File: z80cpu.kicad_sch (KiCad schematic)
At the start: 2 parts

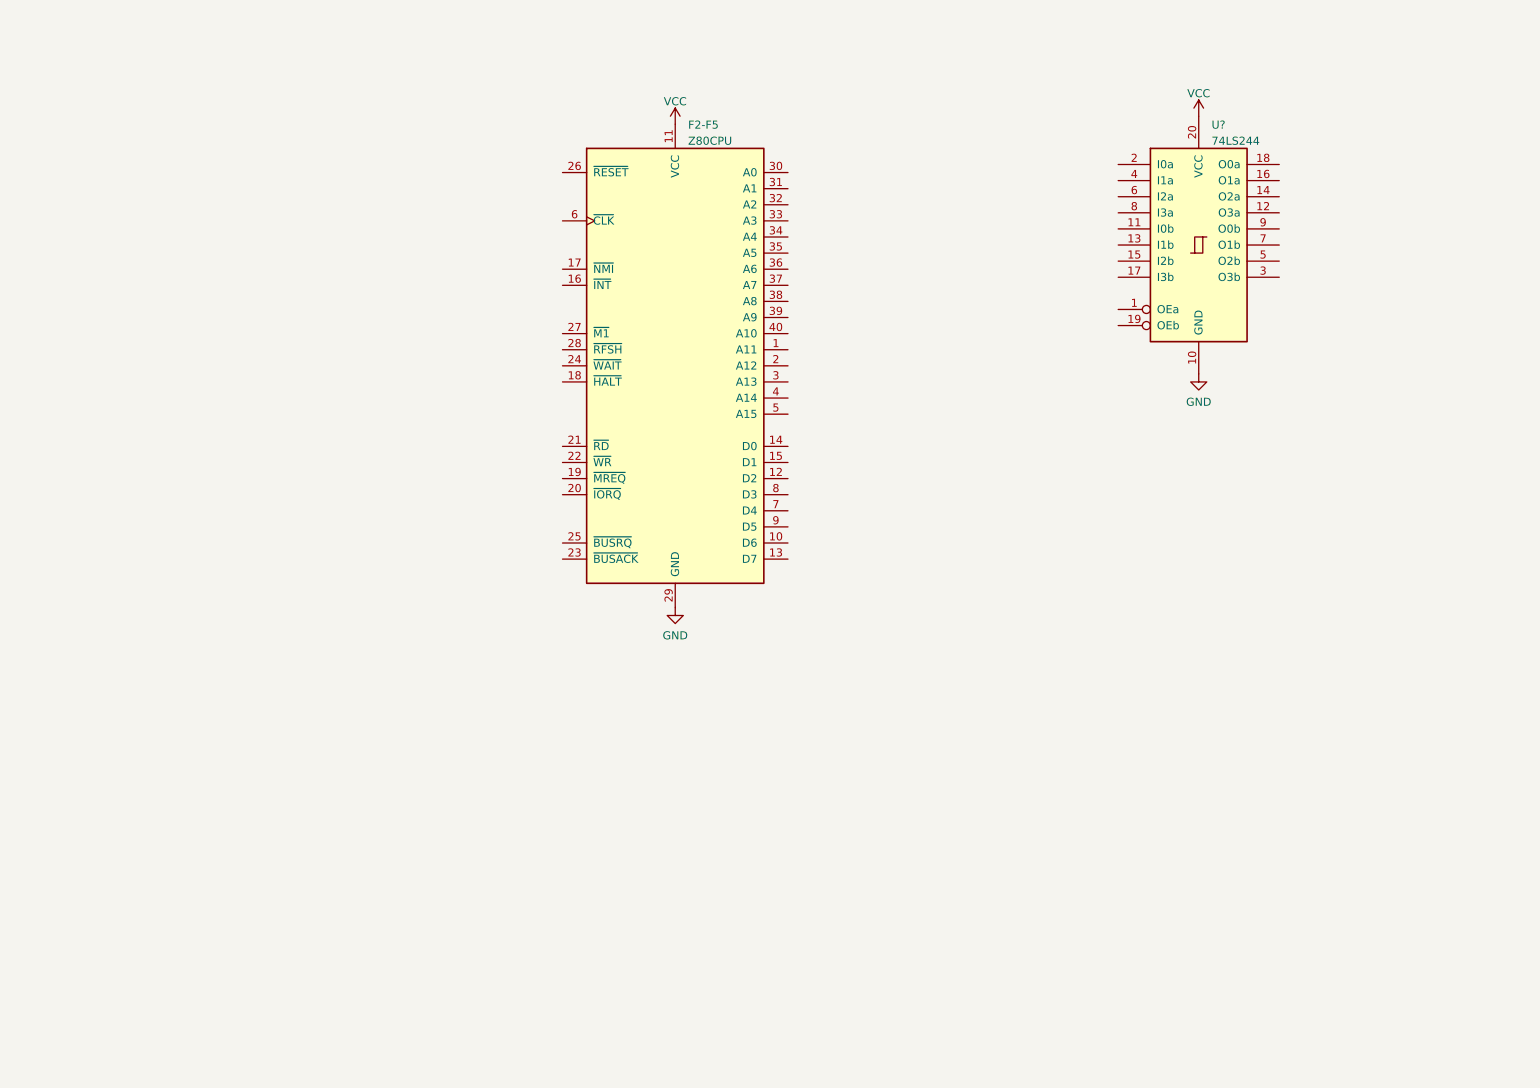
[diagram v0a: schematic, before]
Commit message: Added bus buffers (or their placeholders) to z80cpu schematic
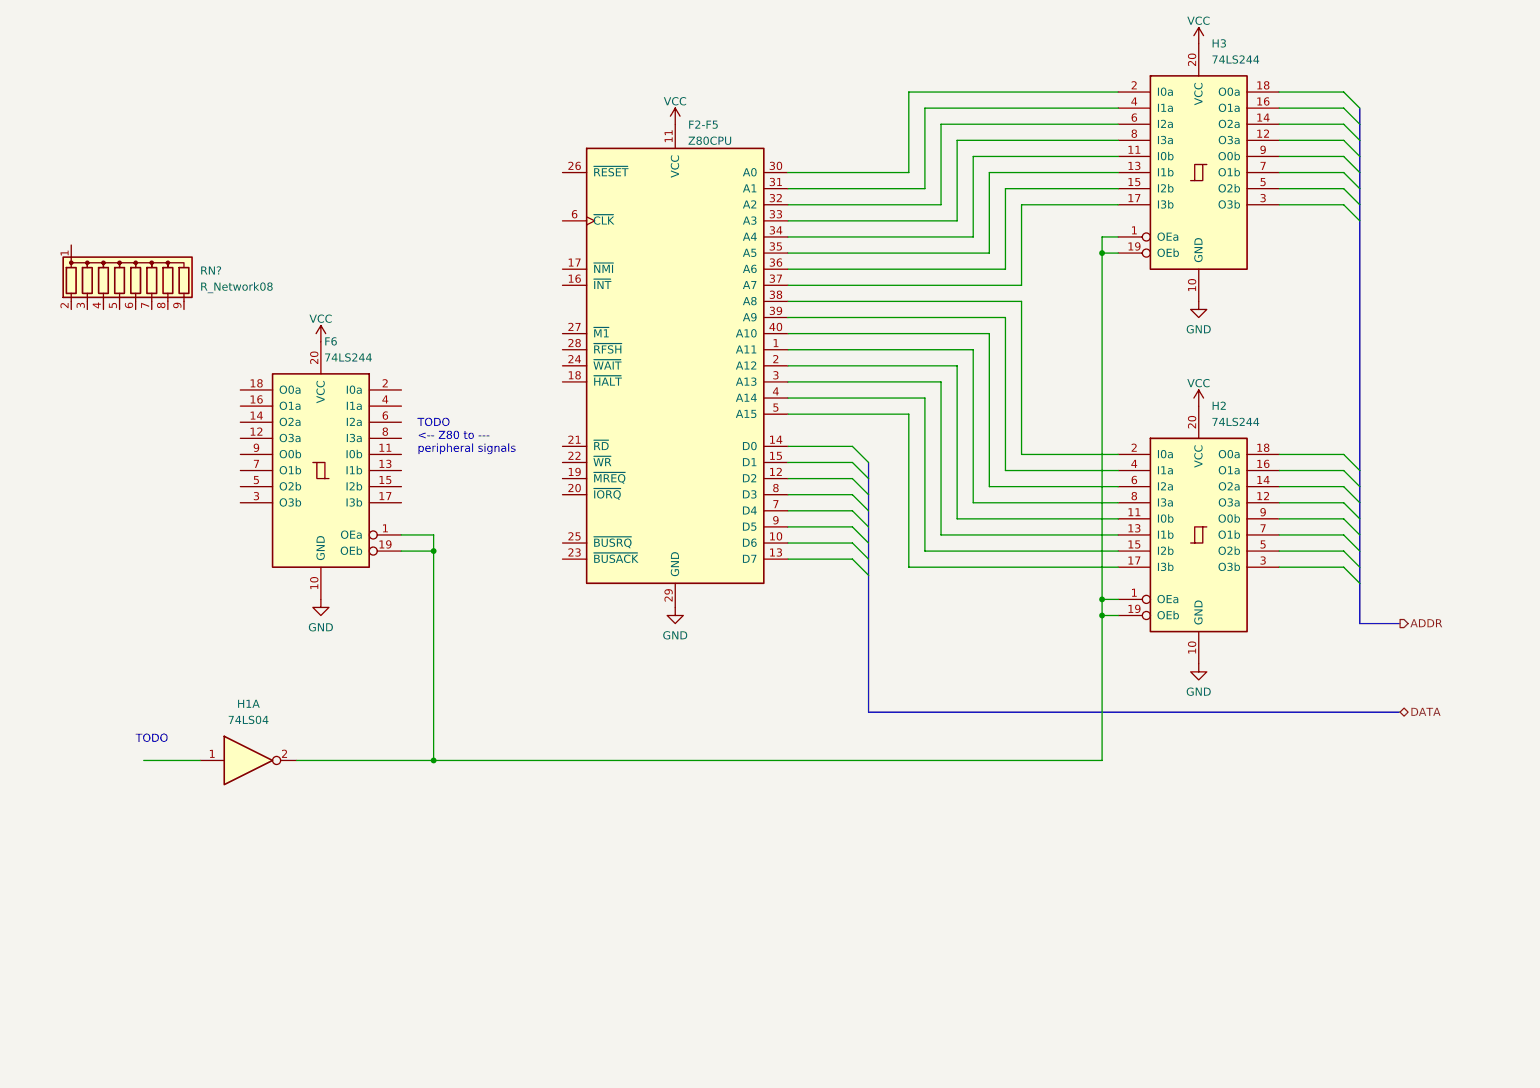
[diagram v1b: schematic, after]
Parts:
- added F6, H2: 74LS244, symbol 74xx:74LS244
- added H1: 74LS04, symbol 74xx:74LS04
- added RN?: R_Network08, Resistor_THT:R_Array_SIP9, symbol Device:R_Network08
- gave numbers to parts that had none: 1
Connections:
- net GND: now also F6.10 (GND), H2.10 (GND)
- net VCC: now also F6.20 (VCC), H2.20 (VCC)
- net at H3.1 (OEa): now also H3.19 (OEb), F6.1 (OEa), F6.19 (OEb), H1.2, H2.1 (OEa), H2.19 (OEb)
- net at H3.11 (I0b): now also F2-F5.34 (A4)
- net at H3.13 (I1b): now also F2-F5.35 (A5)
- net at H3.15 (I2b): now also F2-F5.36 (A6)
- net at H3.17 (I3b): now also F2-F5.37 (A7)
- net at H3.2 (I0a): now also F2-F5.30 (A0)
- net at H3.4 (I1a): now also F2-F5.31 (A1)
- net at H3.6 (I2a): now also F2-F5.32 (A2)
- net at H3.8 (I3a): now also F2-F5.33 (A3)
- net at F2-F5.1 (A11): now also H2.8 (I3a)
- net at F2-F5.2 (A12): now also H2.11 (I0b)
- net at F2-F5.3 (A13): now also H2.13 (I1b)
- net at F2-F5.38 (A8): now also H2.2 (I0a)
- net at F2-F5.39 (A9): now also H2.4 (I1a)
- net at F2-F5.4 (A14): now also H2.15 (I2b)
- net at F2-F5.40 (A10): now also H2.6 (I2a)
- net at F2-F5.5 (A15): now also H2.17 (I3b)
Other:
- note added: "TODO"
- note added: "TODO <-- Z80 to --- peripheral signals"
- moved on the sheet: H3

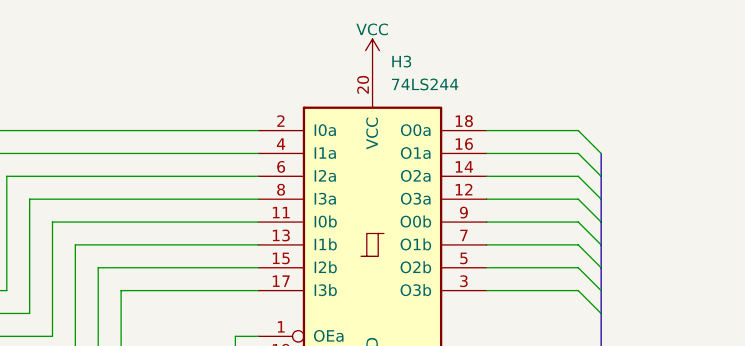
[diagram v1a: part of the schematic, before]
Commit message: Upgraded to kicad 7
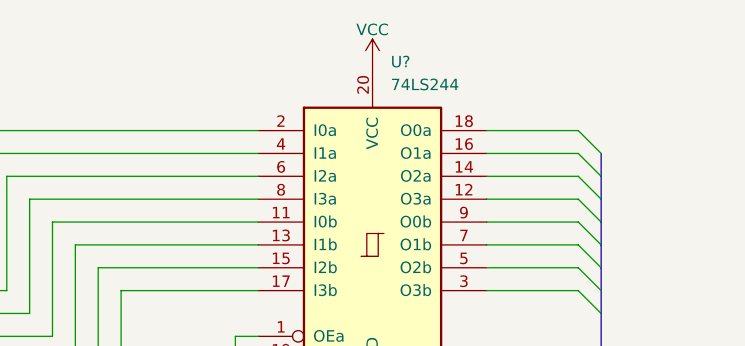
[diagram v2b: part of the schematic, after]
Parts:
- renumbered H3 to U?

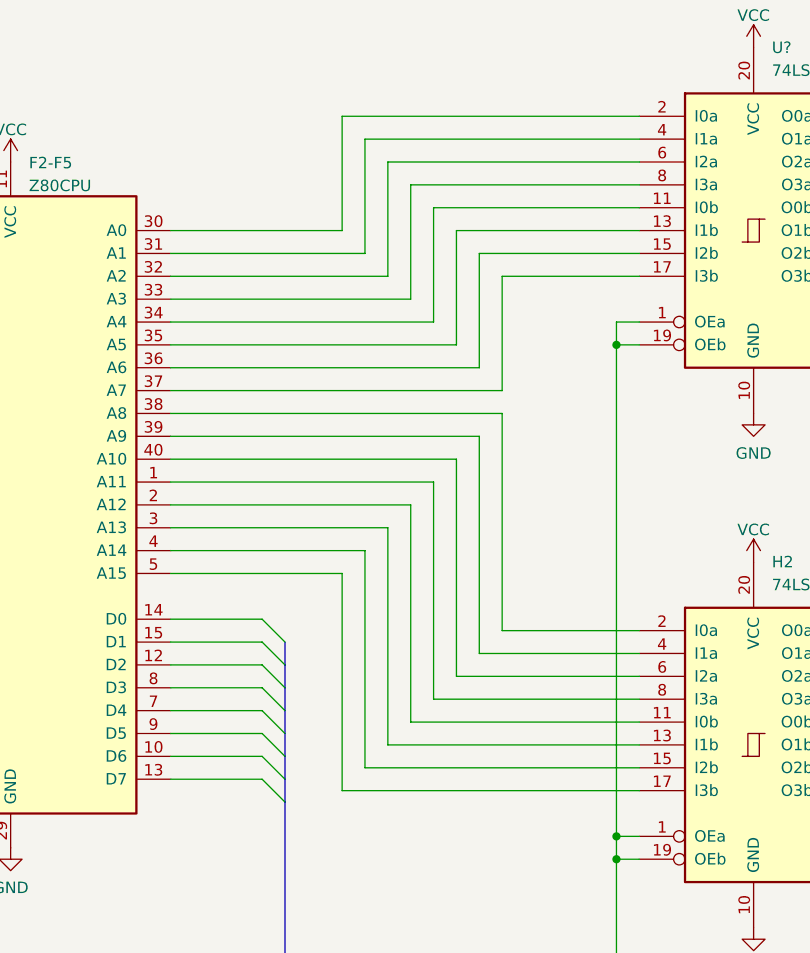
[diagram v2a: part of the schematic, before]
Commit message: Fixed address connection from Z80 to buffers
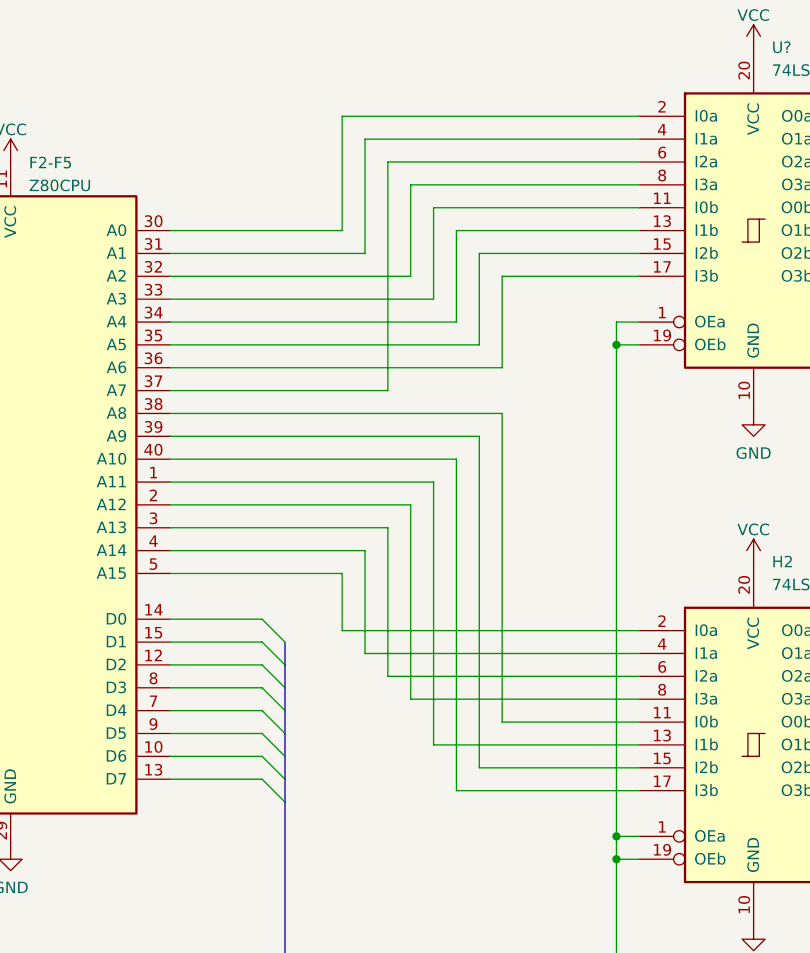
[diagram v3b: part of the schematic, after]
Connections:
- net at U?.11 (I0b): now also F2-F5.33 (A3); no longer F2-F5.34 (A4)
- net at U?.13 (I1b): now also F2-F5.34 (A4); no longer F2-F5.35 (A5)
- net at U?.15 (I2b): now also F2-F5.35 (A5); no longer F2-F5.36 (A6)
- net at U?.17 (I3b): now also F2-F5.36 (A6); no longer F2-F5.37 (A7)
- net at U?.6 (I2a): now also F2-F5.37 (A7); no longer F2-F5.32 (A2)
- net at U?.8 (I3a): now also F2-F5.32 (A2); no longer F2-F5.33 (A3)
- net at F2-F5.1 (A11): now also H2.13 (I1b); no longer H2.8 (I3a)
- net at F2-F5.2 (A12): now also H2.8 (I3a); no longer H2.11 (I0b)
- net at F2-F5.3 (A13): now also H2.6 (I2a); no longer H2.13 (I1b)
- net at F2-F5.38 (A8): now also H2.11 (I0b); no longer H2.2 (I0a)
- net at F2-F5.39 (A9): now also H2.15 (I2b); no longer H2.4 (I1a)
- net at F2-F5.4 (A14): now also H2.4 (I1a); no longer H2.15 (I2b)
- net at F2-F5.40 (A10): now also H2.17 (I3b); no longer H2.6 (I2a)
- net at F2-F5.5 (A15): now also H2.2 (I0a); no longer H2.17 (I3b)
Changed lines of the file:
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@@
     (stroke (width 0) (type default))
   )
-  (wire (pts (xy 185.42 99.06) (xy 157.48 99.06))
+  (wire (pts (xy 185.42 99.06) (xy 162.56 99.06))
     (stroke (width 0) (type default))
   )
@@
     (stroke (width 0) (type default))
   )
-  (wire (pts (xy 154.94 101.6) (xy 185.42 101.6))
+  (wire (pts (xy 157.48 91.44) (xy 157.48 74.93))
     (stroke (width 0) (type default))
   )
@@
     (stroke (width 0) (type default))
   )
-  (wire (pts (xy 170.18 46.99) (xy 170.18 59.69))
+  (wire (pts (xy 170.18 46.99) (xy 170.18 57.15))
     (stroke (width 0) (type default))
   )
@@
     (stroke (width 0) (type default))
   )
+  (wire (pts (xy 160.02 46.99) (xy 160.02 36.83))
+    (stroke (width 0) (type default))
+  )
   (bus (pts (xy 146.05 105.41) (xy 146.05 127))
     (stroke (width 0) (type default))
   )
+  (wire (pts (xy 162.56 49.53) (xy 162.56 39.37))
+    (stroke (width 0) (type default))
+  )
+  (wire (pts (xy 170.18 96.52) (xy 185.42 96.52))
+    (stroke (width 0) (type default))
+  )
+  (wire (pts (xy 170.18 62.23) (xy 170.18 96.52))
+    (stroke (width 0) (type default))
+  )
+  (wire (pts (xy 133.35 49.53) (xy 162.56 49.53))
+    (stroke (width 0) (type default))
+  )
   (wire (pts (xy 167.64 64.77) (xy 133.35 64.77))
     (stroke (width 0) (type default))
@@
     (stroke (width 0) (type default))
   )
-  (wire (pts (xy 133.35 49.53) (xy 160.02 49.53))
-    (stroke (width 0) (type default))
-  )
   (wire (pts (xy 152.4 29.21) (xy 185.42 29.21))
     (stroke (width 0) (type default))
@@
     (stroke (width 0) (type default))
   )
-  (wire (pts (xy 167.64 88.9) (xy 167.64 64.77))
-    (stroke (width 0) (type default))
-  )
   (wire (pts (xy 185.42 52.07) (xy 182.88 52.07))
     (stroke (width 0) (type default))
   )
-  (wire (pts (xy 160.02 72.39) (xy 160.02 96.52))
+  (wire (pts (xy 160.02 72.39) (xy 160.02 93.98))
     (stroke (width 0) (type default))
   )
@@
     (stroke (width 0) (type default))
   )
-  (wire (pts (xy 162.56 93.98) (xy 162.56 69.85))
-    (stroke (width 0) (type default))
-  )
-  (wire (pts (xy 170.18 59.69) (xy 133.35 59.69))
-    (stroke (width 0) (type default))
-  )
   (bus (pts (xy 223.52 39.37) (xy 223.52 41.91))
     (stroke (width 0) (type default))
@@
     (stroke (width 0) (type default))
   )
-  (wire (pts (xy 185.42 104.14) (xy 152.4 104.14))
+  (wire (pts (xy 167.64 64.77) (xy 167.64 101.6))
+    (stroke (width 0) (type default))
+  )
+  (wire (pts (xy 185.42 104.14) (xy 165.1 104.14))
     (stroke (width 0) (type default))
   )
@@
     (stroke (width 0) (type default))
   )
+  (wire (pts (xy 152.4 86.36) (xy 152.4 80.01))
+    (stroke (width 0) (type default))
+  )
   (wire (pts (xy 182.88 52.07) (xy 182.88 54.61))
     (stroke (width 0) (type default))
@@
     (stroke (width 0) (type default))
   )
-  (wire (pts (xy 185.42 93.98) (xy 162.56 93.98))
-    (stroke (width 0) (type default))
-  )
-  (wire (pts (xy 157.48 46.99) (xy 133.35 46.99))
-    (stroke (width 0) (type default))
-  )
   (bus (pts (xy 223.52 44.45) (xy 223.52 46.99))
     (stroke (width 0) (type default))
@@
     (stroke (width 0) (type default))
   )
-  (wire (pts (xy 160.02 96.52) (xy 185.42 96.52))
-    (stroke (width 0) (type default))
-  )
-  (wire (pts (xy 165.1 54.61) (xy 133.35 54.61))
+  (wire (pts (xy 133.35 54.61) (xy 167.64 54.61))
     (stroke (width 0) (type default))
   )
@@
     (stroke (width 0) (type default))
   )
-  (wire (pts (xy 165.1 41.91) (xy 165.1 54.61))
+  (wire (pts (xy 165.1 41.91) (xy 165.1 52.07))
     (stroke (width 0) (type default))
   )
@@
     (stroke (width 0) (type default))
   )
-  (wire (pts (xy 157.48 99.06) (xy 157.48 74.93))
-    (stroke (width 0) (type default))
-  )
   (wire (pts (xy 210.82 31.75) (xy 220.98 31.75))
     (stroke (width 0) (type default))
@@
     (stroke (width 0) (type default))
   )
-  (wire (pts (xy 170.18 62.23) (xy 170.18 86.36))
-    (stroke (width 0) (type default))
-  )
   (wire (pts (xy 133.35 90.17) (xy 143.51 90.17))
     (stroke (width 0) (type default))
@@
     (stroke (width 0) (type default))
   )
-  (wire (pts (xy 133.35 57.15) (xy 167.64 57.15))
-    (stroke (width 0) (type default))
-  )
-  (wire (pts (xy 160.02 49.53) (xy 160.02 36.83))
+  (wire (pts (xy 133.35 57.15) (xy 170.18 57.15))
     (stroke (width 0) (type default))
   )
@@
     (stroke (width 0) (type default))
   )
-  (wire (pts (xy 165.1 67.31) (xy 165.1 91.44))
-    (stroke (width 0) (type default))
-  )
-  (wire (pts (xy 167.64 57.15) (xy 167.64 44.45))
+  (wire (pts (xy 165.1 67.31) (xy 165.1 104.14))
     (stroke (width 0) (type default))
   )
@@
     (stroke (width 0) (type default))
   )
-  (wire (pts (xy 152.4 104.14) (xy 152.4 80.01))
-    (stroke (width 0) (type default))
-  )
   (bus (pts (xy 223.52 88.9) (xy 223.52 91.44))
     (stroke (width 0) (type default))
@@
     (stroke (width 0) (type default))
   )
+  (wire (pts (xy 167.64 101.6) (xy 185.42 101.6))
+    (stroke (width 0) (type default))
+  )
+  (wire (pts (xy 162.56 69.85) (xy 162.56 99.06))
+    (stroke (width 0) (type default))
+  )
   (wire (pts (xy 133.35 41.91) (xy 152.4 41.91))
     (stroke (width 0) (type default))
@@
     (stroke (width 0) (type default))
   )
-  (wire (pts (xy 170.18 86.36) (xy 185.42 86.36))
+  (wire (pts (xy 152.4 86.36) (xy 185.42 86.36))
+    (stroke (width 0) (type default))
+  )
+  (wire (pts (xy 167.64 54.61) (xy 167.64 44.45))
     (stroke (width 0) (type default))
   )
@@
     (stroke (width 0) (type default))
   )
-  (wire (pts (xy 154.94 77.47) (xy 154.94 101.6))
-    (stroke (width 0) (type default))
-  )
-  (wire (pts (xy 133.35 52.07) (xy 162.56 52.07))
+  (wire (pts (xy 154.94 77.47) (xy 154.94 88.9))
+    (stroke (width 0) (type default))
+  )
+  (wire (pts (xy 133.35 52.07) (xy 165.1 52.07))
     (stroke (width 0) (type default))
   )
@@
     (stroke (width 0) (type default))
   )
+  (wire (pts (xy 160.02 93.98) (xy 185.42 93.98))
+    (stroke (width 0) (type default))
+  )
   (bus (pts (xy 223.52 36.83) (xy 223.52 39.37))
     (stroke (width 0) (type default))
@@
     (stroke (width 0) (type default))
   )
-  (wire (pts (xy 185.42 88.9) (xy 167.64 88.9))
+  (wire (pts (xy 154.94 88.9) (xy 185.42 88.9))
     (stroke (width 0) (type default))
   )
@@
     (stroke (width 0) (type default))
   )
+  (wire (pts (xy 133.35 46.99) (xy 160.02 46.99))
+    (stroke (width 0) (type default))
+  )
   (wire (pts (xy 133.35 44.45) (xy 154.94 44.45))
     (stroke (width 0) (type default))
@@
     (stroke (width 0) (type default))
   )
-  (wire (pts (xy 157.48 34.29) (xy 157.48 46.99))
-    (stroke (width 0) (type default))
-  )
   (wire (pts (xy 157.48 74.93) (xy 133.35 74.93))
     (stroke (width 0) (type default))
@@
     (stroke (width 0) (type default))
   )
-  (wire (pts (xy 165.1 91.44) (xy 185.42 91.44))
-    (stroke (width 0) (type default))
-  )
-  (wire (pts (xy 162.56 52.07) (xy 162.56 39.37))
+  (wire (pts (xy 157.48 91.44) (xy 185.42 91.44))
+    (stroke (width 0) (type default))
+  )
+  (wire (pts (xy 157.48 34.29) (xy 157.48 59.69))
     (stroke (width 0) (type default))
   )
@@
     (stroke (width 0) (type default))
   )
+  (wire (pts (xy 157.48 59.69) (xy 133.35 59.69))
+    (stroke (width 0) (type default))
+  )
